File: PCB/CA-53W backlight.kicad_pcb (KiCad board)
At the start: 2 copper layers, 11.4 x 10.4 mm, 10 parts

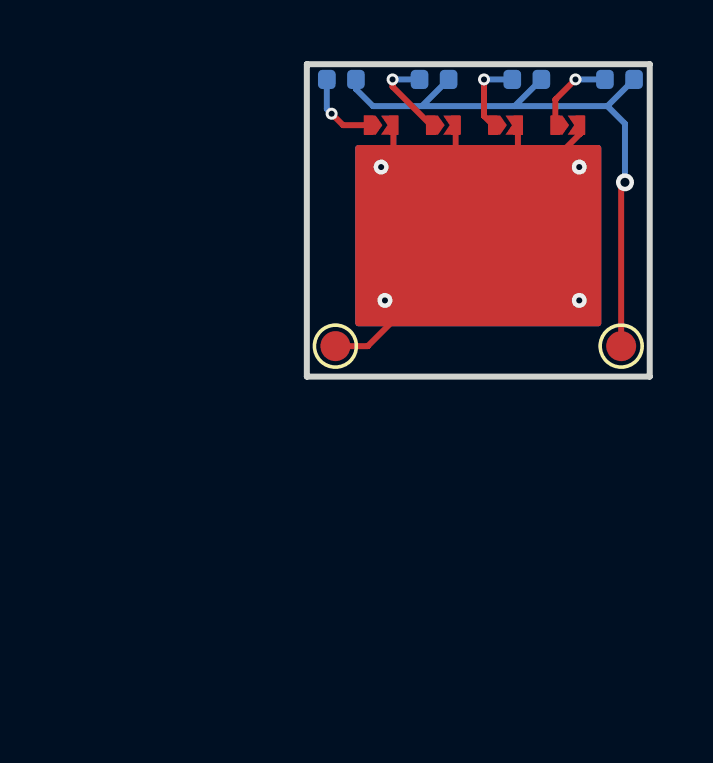
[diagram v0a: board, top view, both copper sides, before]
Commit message: image and press button layout
adding image for ref and starting to lay out press button
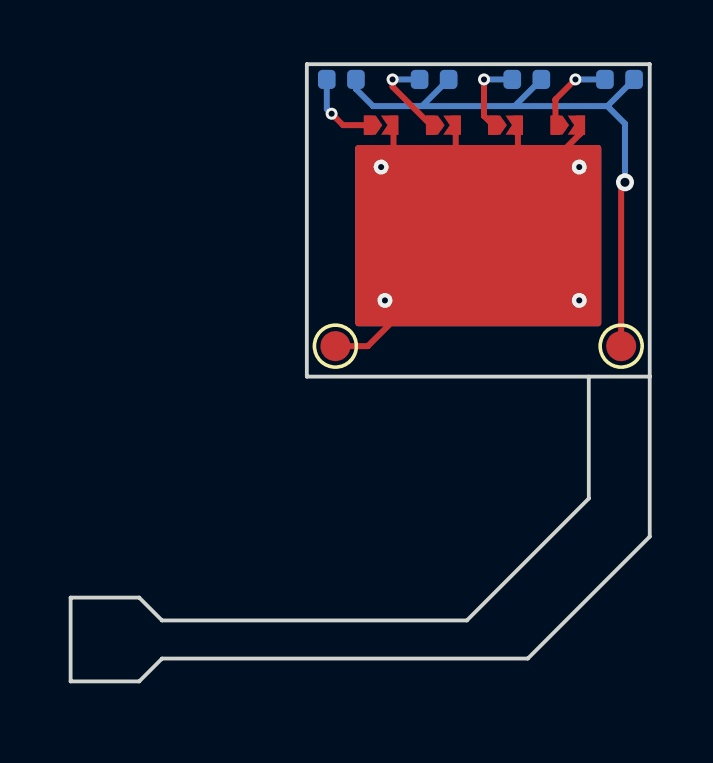
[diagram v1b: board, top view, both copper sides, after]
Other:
- board size 11.4 x 10.4 mm -> 19.3 x 20.6 mm
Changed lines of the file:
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@@
 		(allow_soldermask_bridges_in_footprints no)
 		(aux_axis_origin 138 96.25)
-		(grid_origin 139.7145 94.472)
+		(grid_origin 149.43 96.25)
 		(pcbplotparams
 			(layerselection 0x00010fc_ffffffff)
@@
 		(net 6)
 	)
+	(gr_line
+		(start 132.412 103.616)
+		(end 133.174 104.378)
+		(stroke
+			(width 0.127)
+			(type default)
+		)
+		(layer "Edge.Cuts")
+	)
+	(gr_line
+		(start 130.126 103.616)
+		(end 132.412 103.616)
+		(stroke
+			(width 0.127)
+			(type default)
+		)
+		(layer "Edge.Cuts")
+	)
+	(gr_line
+		(start 130.126 106.41)
+		(end 130.126 103.616)
+		(stroke
+			(width 0.127)
+			(type default)
+		)
+		(layer "Edge.Cuts")
+	)
+	(gr_line
+		(start 133.174 105.648)
+		(end 145.366 105.648)
+		(stroke
+			(width 0.127)
+			(type default)
+		)
+		(layer "Edge.Cuts")
+	)
+	(gr_line
+		(start 149.43 96.25)
+		(end 149.43 101.584)
+		(stroke
+			(width 0.127)
+			(type default)
+		)
+		(layer "Edge.Cuts")
+	)
+	(gr_line
+		(start 143.334 104.378)
+		(end 147.398 100.314)
+		(stroke
+			(width 0.127)
+			(type default)
+		)
+		(layer "Edge.Cuts")
+	)
+	(gr_line
+		(start 145.366 105.648)
+		(end 149.43 101.584)
+		(stroke
+			(width 0.127)
+			(type default)
+		)
+		(layer "Edge.Cuts")
+	)
+	(gr_line
+		(start 132.412 106.41)
+		(end 133.174 105.648)
+		(stroke
+			(width 0.127)
+			(type default)
+		)
+		(layer "Edge.Cuts")
+	)
+	(gr_line
+		(start 132.412 106.41)
+		(end 130.126 106.41)
+		(stroke
+			(width 0.127)
+			(type default)
+		)
+		(layer "Edge.Cuts")
+	)
 	(gr_rect
 		(start 138 85.836)
 		(end 149.43 96.25)
 		(stroke
-			(width 0.2)
+			(width 0.127)
 			(type default)
 		)
@@
 		(layer "Edge.Cuts")
 	)
+	(gr_line
+		(start 147.398 100.314)
+		(end 147.398 96.25)
+		(stroke
+			(width 0.127)
+			(type default)
+		)
+		(layer "Edge.Cuts")
+	)
+	(gr_line
+		(start 133.174 104.378)
+		(end 143.334 104.378)
+		(stroke
+			(width 0.127)
+			(type default)
+		)
+		(layer "Edge.Cuts")
+	)

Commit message: Out for boards Rev A
getting quoted through JLC PCB
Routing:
- net GND: track 21.0 -> 76.2 mm, vias 1 -> 4
- net +3V0: vias 4 -> 5
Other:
- board size 19.3 x 20.6 mm -> 19.6 x 21.3 mm
